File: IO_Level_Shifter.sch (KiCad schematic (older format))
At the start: 29 parts, among them J29 Conn_01x04_Male, J30 Conn_01x04_Male, J31 Conn_01x04_Male, J32 Conn_01x04_Male, J33 Conn_01x04_Male, J34 Conn_01x04_Male, J35 Conn_01x04_Male, J36 Conn_01x04_Male, J37 Conn_01x04_Male, J38 Conn_01x04_Male, J39 Conn_01x04_Male, J40 Conn_01x04_Male, J41 Conn_01x04_Male, J42 Conn_01x04_Male, J43 Conn_01x04_Male, J44 Conn_01x04_Male, J45 Conn_01x04_Male, U4 SN74LVC8T245DWR, U5 SN74LVC8T245DWR, U6 SN74LVC8T245DWR, U7 SN74LVC8T245DWR

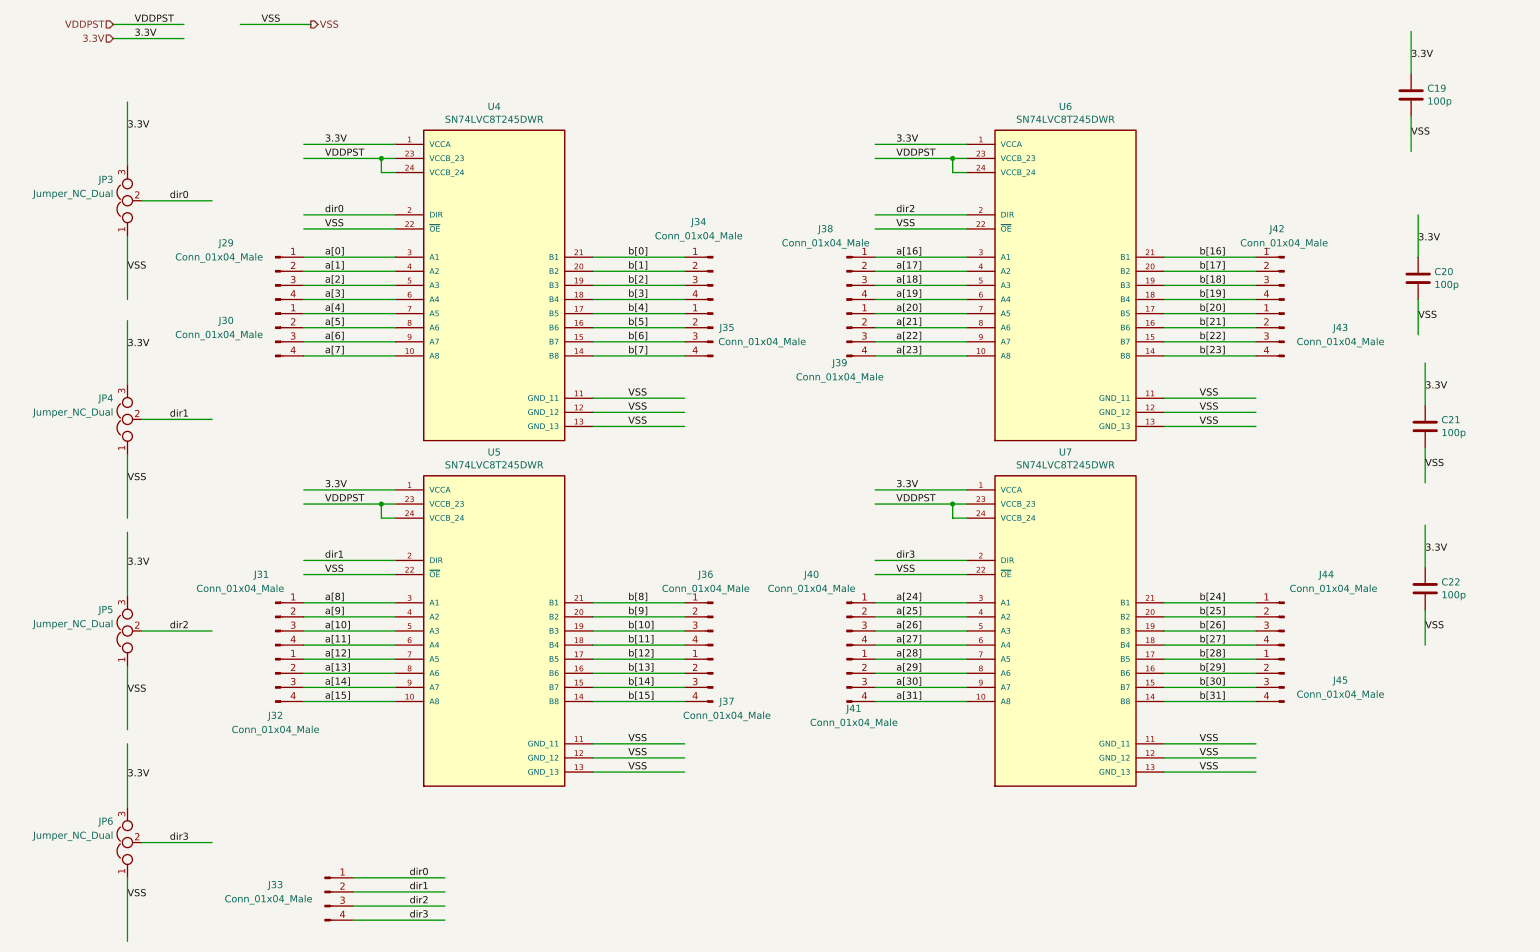
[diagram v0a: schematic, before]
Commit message: ver 4.0: added 1.8V pin
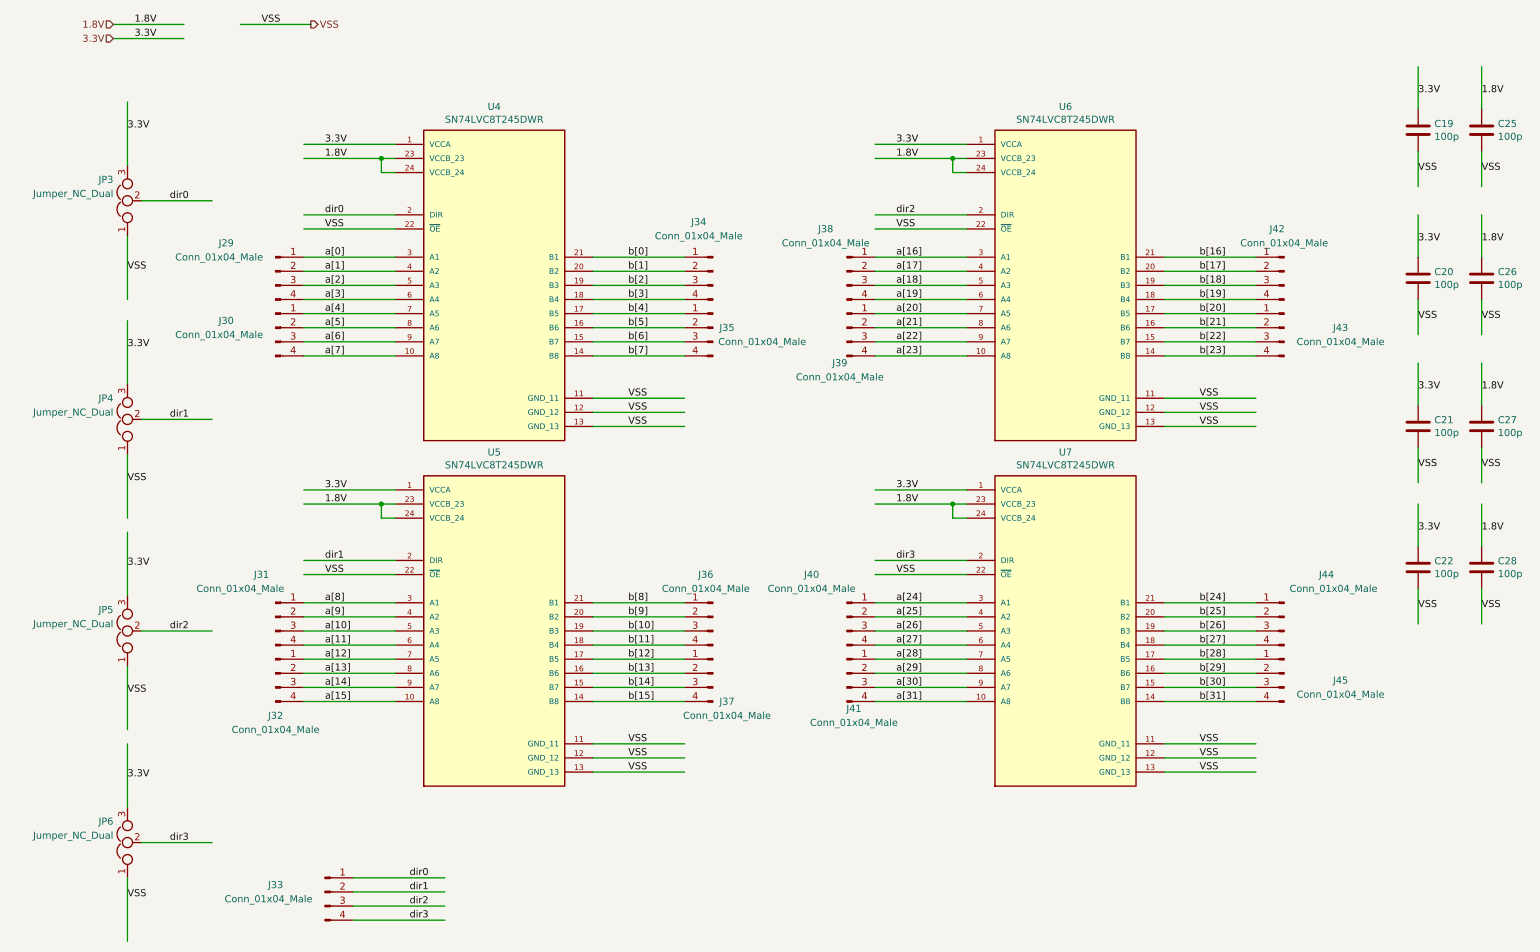
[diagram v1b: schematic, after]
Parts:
- added C25, C26, C27, C28: 100p, Capacitor_SMD:C_0805_2012Metric_Pad1.15x1.40mm_HandSolder, symbol Device:C
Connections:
- net labels added: 1.8V
- net labels removed: VDDPST
- wire segments 131 -> 139
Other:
- moved on the sheet: C19, C21, C22
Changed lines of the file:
@@
 $EndDescr
 Text HLabel 1150 850  0    50   Input ~ 0
-VDDPST
+1.8V
 Text HLabel 1150 950  0    50   Input ~ 0
 3.3V
@@
 	1250 1850 1250 1400
 Text Label 1300 850  0    50   ~ 0
-VDDPST
+1.8V
 Text Label 1300 950  0    50   ~ 0
 3.3V
@@
 L Device:C C19
 U 1 1 6170A9B4
-P 10350 1350
-F 0 "C19" H 10465 1396 50  0000 L CNN
-F 1 "100p" H 10465 1305 50  0000 L CNN
-F 2 "Capacitor_SMD:C_0805_2012Metric_Pad1.15x1.40mm_HandSolder" H 10388 1200 50  0001 C CNN
-F 3 "~" H 10350 1350 50  0001 C CNN
-	1    10350 1350
-	1    0    0    -1
-$EndComp
-Text Label 10350 1650 0    50   ~ 0
-VSS
-Text Label 10350 1100 0    50   ~ 0
-3.3V
-Wire Wire Line
-	10350 1500 10350 1750
-Wire Wire Line
-	10350 1200 10350 900
+P 10400 1600
+F 0 "C19" H 10515 1646 50  0000 L CNN
+F 1 "100p" H 10515 1555 50  0000 L CNN
+F 2 "Capacitor_SMD:C_0805_2012Metric_Pad1.15x1.40mm_HandSolder" H 10438 1450 50  0001 C CNN
+F 3 "~" H 10400 1600 50  0001 C CNN
+	1    10400 1600
+	1    0    0    -1
+$EndComp
+Text Label 10400 1900 0    50   ~ 0
+VSS
+Text Label 10400 1350 0    50   ~ 0
+3.3V
+Wire Wire Line
+	10400 1750 10400 2000
+Wire Wire Line
+	10400 1450 10400 1150
 $Comp
 L Device:C C22
 U 1 1 61708E93
-P 10450 4850
-F 0 "C22" H 10565 4896 50  0000 L CNN
-F 1 "100p" H 10565 4805 50  0000 L CNN
-F 2 "Capacitor_SMD:C_0805_2012Metric_Pad1.15x1.40mm_HandSolder" H 10488 4700 50  0001 C CNN
-F 3 "~" H 10450 4850 50  0001 C CNN
-	1    10450 4850
-	1    0    0    -1
-$EndComp
-Text Label 10450 5150 0    50   ~ 0
-VSS
-Text Label 10450 4600 0    50   ~ 0
-3.3V
-Wire Wire Line
-	10450 5000 10450 5250
-Wire Wire Line
-	10450 4700 10450 4400
+P 10400 4700
+F 0 "C22" H 10515 4746 50  0000 L CNN
+F 1 "100p" H 10515 4655 50  0000 L CNN
+F 2 "Capacitor_SMD:C_0805_2012Metric_Pad1.15x1.40mm_HandSolder" H 10438 4550 50  0001 C CNN
+F 3 "~" H 10400 4700 50  0001 C CNN
+	1    10400 4700
+	1    0    0    -1
+$EndComp
+Text Label 10400 5000 0    50   ~ 0
+VSS
+Text Label 10400 4450 0    50   ~ 0
+3.3V
+Wire Wire Line
+	10400 4850 10400 5100
+Wire Wire Line
+	10400 4550 10400 4250
 $Comp
 L Device:C C21
 U 1 1 617058A9
-P 10450 3700
-F 0 "C21" H 10565 3746 50  0000 L CNN
-F 1 "100p" H 10565 3655 50  0000 L CNN
-F 2 "Capacitor_SMD:C_0805_2012Metric_Pad1.15x1.40mm_HandSolder" H 10488 3550 50  0001 C CNN
-F 3 "~" H 10450 3700 50  0001 C CNN
-	1    10450 3700
-	1    0    0    -1
-$EndComp
-Text Label 10450 4000 0    50   ~ 0
-VSS
-Text Label 10450 3450 0    50   ~ 0
-3.3V
-Wire Wire Line
-	10450 3850 10450 4100
-Wire Wire Line
-	10450 3550 10450 3250
+P 10400 3700
+F 0 "C21" H 10515 3746 50  0000 L CNN
+F 1 "100p" H 10515 3655 50  0000 L CNN
+F 2 "Capacitor_SMD:C_0805_2012Metric_Pad1.15x1.40mm_HandSolder" H 10438 3550 50  0001 C CNN
+F 3 "~" H 10400 3700 50  0001 C CNN
+	1    10400 3700
+	1    0    0    -1
+$EndComp
+Text Label 10400 4000 0    50   ~ 0
+VSS
+Text Label 10400 3450 0    50   ~ 0
+3.3V
+Wire Wire Line
+	10400 3850 10400 4100
+Wire Wire Line
+	10400 3550 10400 3250
 Text Label 2650 1700 0    50   ~ 0
 3.3V
 Text Label 2650 1800 0    50   ~ 0
-VDDPST
+1.8V
 Text Label 2650 2300 0    50   ~ 0
 VSS
@@
 3.3V
 Text Label 6700 1800 0    50   ~ 0
-VDDPST
+1.8V
 Text Label 6700 2300 0    50   ~ 0
 VSS
@@
 3.3V
 Text Label 2650 4250 0    50   ~ 0
-VDDPST
+1.8V
 Text Label 2650 4750 0    50   ~ 0
 VSS
@@
 3.3V
 Text Label 6700 4250 0    50   ~ 0
-VDDPST
+1.8V
 Text Label 6700 4750 0    50   ~ 0
 VSS
@@
 Text Label 3250 7200 0    50   ~ 0
 dir3
+$Comp
+L Device:C C26
+U 1 1 61783856
+P 10850 2650
+F 0 "C26" H 10965 2696 50  0000 L CNN
+F 1 "100p" H 10965 2605 50  0000 L CNN
+F 2 "Capacitor_SMD:C_0805_2012Metric_Pad1.15x1.40mm_HandSolder" H 10888 2500 50  0001 C CNN
+F 3 "~" H 10850 2650 50  0001 C CNN
+	1    10850 2650
+	1    0    0    -1
+$EndComp
+Text Label 10850 2950 0    50   ~ 0
+VSS
+Text Label 10850 2400 0    50   ~ 0
+1.8V
+Wire Wire Line
+	10850 2800 10850 3050
+Wire Wire Line
+	10850 2500 10850 2200
+$Comp
+L Device:C C25
+U 1 1 61783864
+P 10850 1600
+F 0 "C25" H 10965 1646 50  0000 L CNN
+F 1 "100p" H 10965 1555 50  0000 L CNN
+F 2 "Capacitor_SMD:C_0805_2012Metric_Pad1.15x1.40mm_HandSolder" H 10888 1450 50  0001 C CNN
+F 3 "~" H 10850 1600 50  0001 C CNN
+	1    10850 1600
+	1    0    0    -1
+$EndComp
+Text Label 10850 1900 0    50   ~ 0
+VSS
+Text Label 10850 1350 0    50   ~ 0
+1.8V
+Wire Wire Line
+	10850 1750 10850 2000
+Wire Wire Line
+	10850 1450 10850 1150
+$Comp
+L Device:C C28
+U 1 1 61783872
+P 10850 4700
+F 0 "C28" H 10965 4746 50  0000 L CNN
+F 1 "100p" H 10965 4655 50  0000 L CNN
+F 2 "Capacitor_SMD:C_0805_2012Metric_Pad1.15x1.40mm_HandSolder" H 10888 4550 50  0001 C CNN
+F 3 "~" H 10850 4700 50  0001 C CNN
+	1    10850 4700
+	1    0    0    -1
+$EndComp
+Text Label 10850 5000 0    50   ~ 0
+VSS
+Text Label 10850 4450 0    50   ~ 0
+1.8V
+Wire Wire Line
+	10850 4850 10850 5100
+Wire Wire Line
+	10850 4550 10850 4250
+$Comp
+L Device:C C27
+U 1 1 61783880
+P 10850 3700
+F 0 "C27" H 10965 3746 50  0000 L CNN
+F 1 "100p" H 10965 3655 50  0000 L CNN
+F 2 "Capacitor_SMD:C_0805_2012Metric_Pad1.15x1.40mm_HandSolder" H 10888 3550 50  0001 C CNN
+F 3 "~" H 10850 3700 50  0001 C CNN
+	1    10850 3700
+	1    0    0    -1
+$EndComp
+Text Label 10850 4000 0    50   ~ 0
+VSS
+Text Label 10850 3450 0    50   ~ 0
+1.8V
+Wire Wire Line
+	10850 3850 10850 4100
+Wire Wire Line
+	10850 3550 10850 3250
 $EndSCHEMATC
